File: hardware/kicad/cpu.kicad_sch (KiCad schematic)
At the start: 18 parts, among them U1 74AC04, U2 74AC245, U3 74AC573, U4 W65C816S, U5 DS1813-5+, X1 MXO45HS

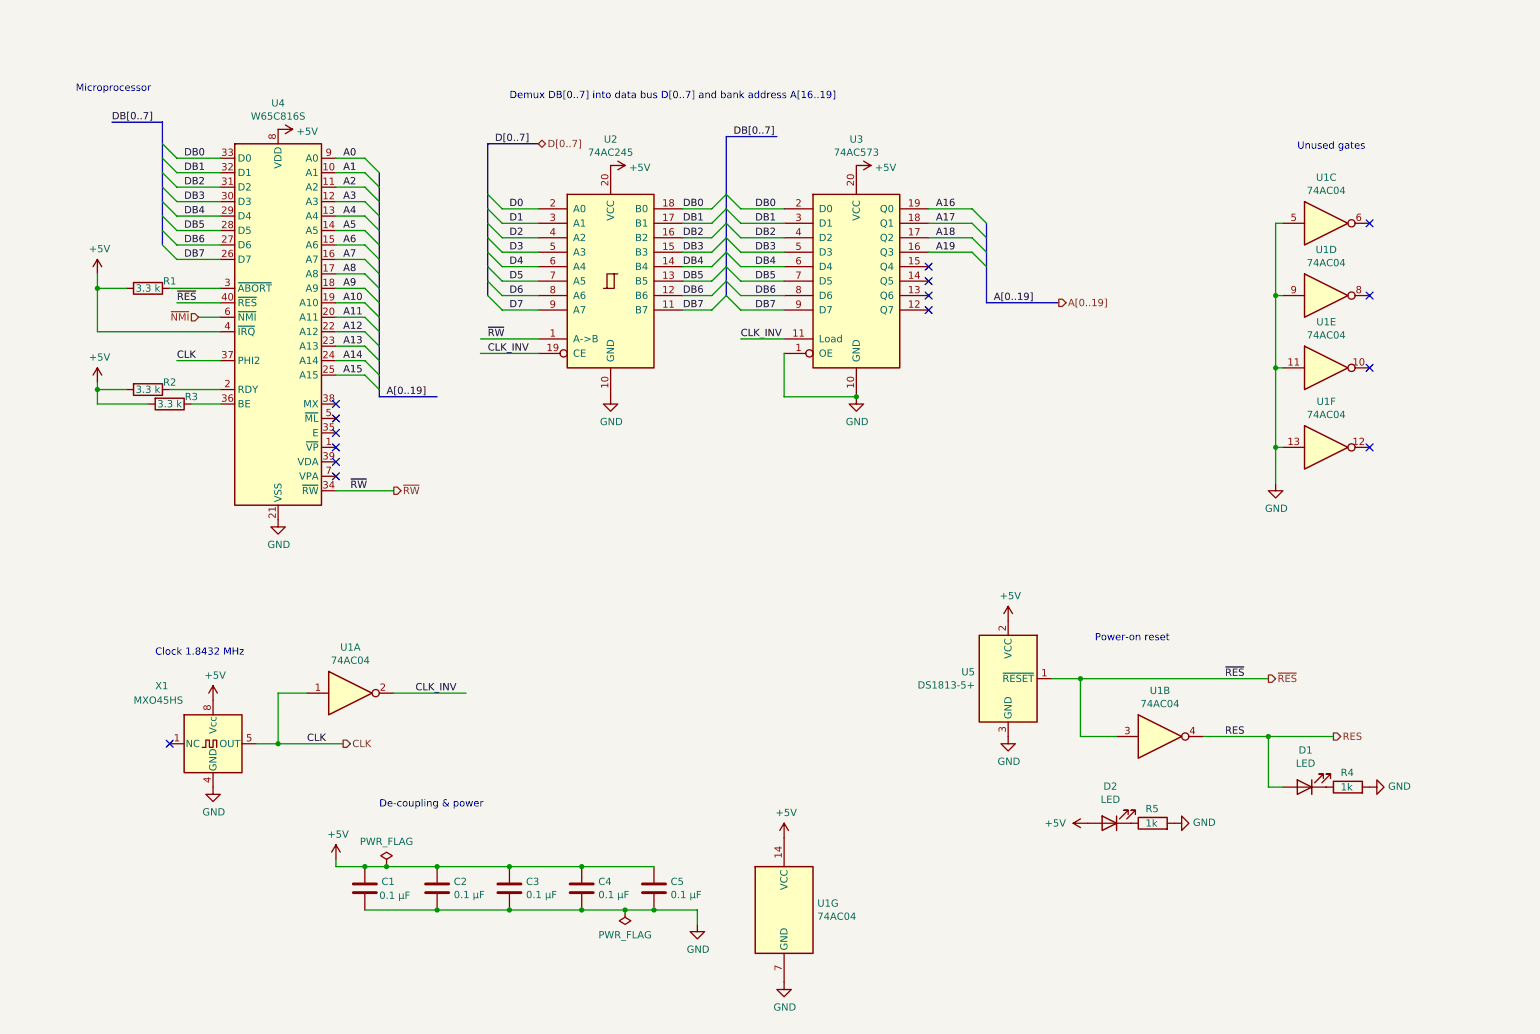
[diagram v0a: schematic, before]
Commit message: update hardware files to match current WIP design
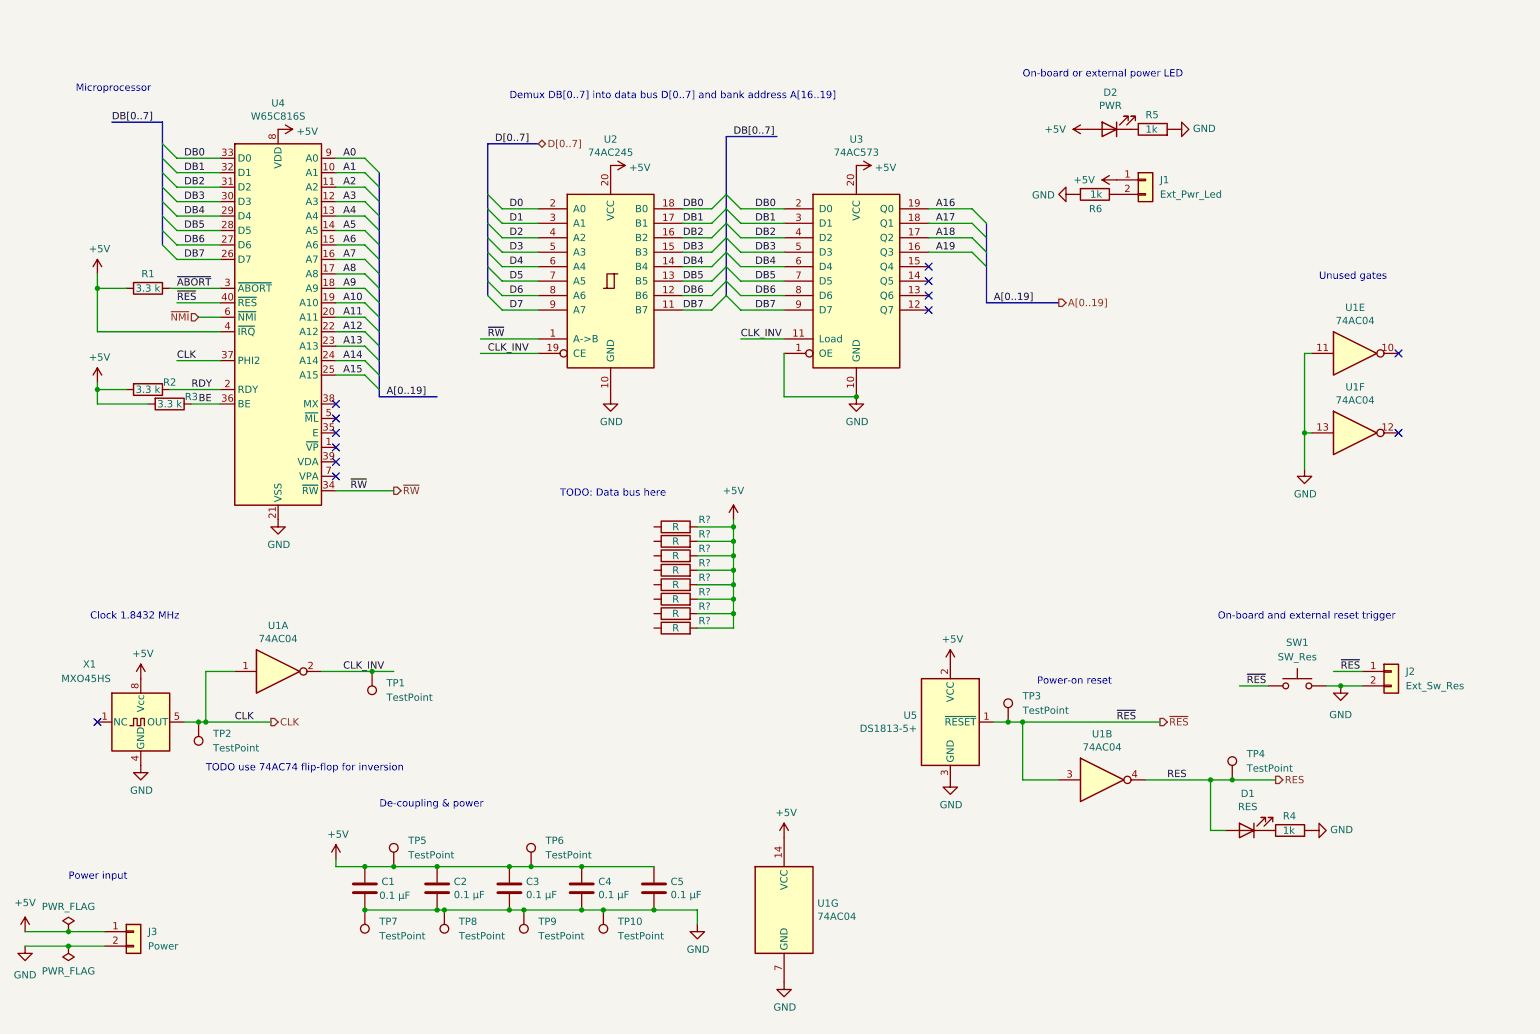
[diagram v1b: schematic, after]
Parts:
- removed unit 3 of U1
- removed unit 4 of U1
- added J1: Ext_Pwr_Led, Connector_PinHeader_2.54mm:PinHeader_1x02_P2.54mm_Vertical, symbol Connector_Generic:Conn_01x02
- added J2: Ext_Sw_Res, Connector_PinHeader_2.54mm:PinHeader_1x02_P2.54mm_Vertical, symbol Connector_Generic:Conn_01x02
- added J3: Power, Connector_PinHeader_2.54mm:PinHeader_1x02_P2.54mm_Vertical, symbol Connector_Generic:Conn_01x02
- added R6: 1k, Resistor_SMD:R_0603_1608Metric_Pad0.98x0.95mm_HandSolder, symbol Device:R
- added R? (x8): R, symbol Device:R
- added SW1: SW_Res, Button_Switch_THT:SW_TH_Tactile_Omron_B3F-10xx, symbol Switch:SW_Push
- added TP1, TP10, TP2, TP3, TP4, TP5, TP6, TP7, TP8, TP9: TestPoint, symbol Connector:TestPoint
- C1, C2, C3, C4, C5: footprint (none) -> Capacitor_SMD:C_0603_1608Metric_Pad1.08x0.95mm_HandSolder
- D1: value LED -> RES; footprint (none) -> LED_SMD:LED_0603_1608Metric_Pad1.05x0.95mm_HandSolder
- D2: value LED -> PWR; footprint (none) -> LED_SMD:LED_0603_1608Metric_Pad1.05x0.95mm_HandSolder
- R1, R2, R3, R4, R5: footprint (none) -> Resistor_SMD:R_0603_1608Metric_Pad0.98x0.95mm_HandSolder
- U1: footprint (none) -> Package_DIP:DIP-14_W7.62mm_Socket
- U2, U3: footprint (none) -> Package_DIP:DIP-20_W7.62mm_Socket
- U5: footprint Package_TO_SOT_SMD:SOT-23 -> Package_TO_SOT_THT:TO-92
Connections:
- net +5V: now also J1.1 (Pin_1), J3.1 (Pin_1), R?.2, R?.2, R?.2, R?.2, R?.2, R?.2, R?.2, R?.2, TP5.1, TP6.1
- net CLK: now also TP2.1
- net CLK_INV: now also TP1.1
- net GND: now also J2.2 (Pin_2), J3.2 (Pin_2), R6.2, SW1.2, TP10.1, TP7.1, TP8.1, TP9.1
- net RES: now also TP4.1
- net ~{RES}: now also J2.1 (Pin_1), SW1.1, TP3.1
- net RDY: now reaches R2.1, U4.2 (RDY)
- net ~{ABORT}: now reaches R1.1, U4.3 (~{ABORT})
- net BE: now reaches R3.1, U4.36 (BE)
- new net: J1.2 (Pin_2), R6.1
- no-connect marks 15 -> 13
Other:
- note added: "On-board and external reset trigger"
- note added: "On-board or external power LED"
- note added: "Power input"
- note added: "TODO use 74AC74 flip-flop for inversion"
- note added: "TODO: Data bus here"
- moved on the sheet: D1, D2, R4, R5, U1A, U1B, U1E, U1F, U5, X1

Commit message: update schematic, add draft PCB
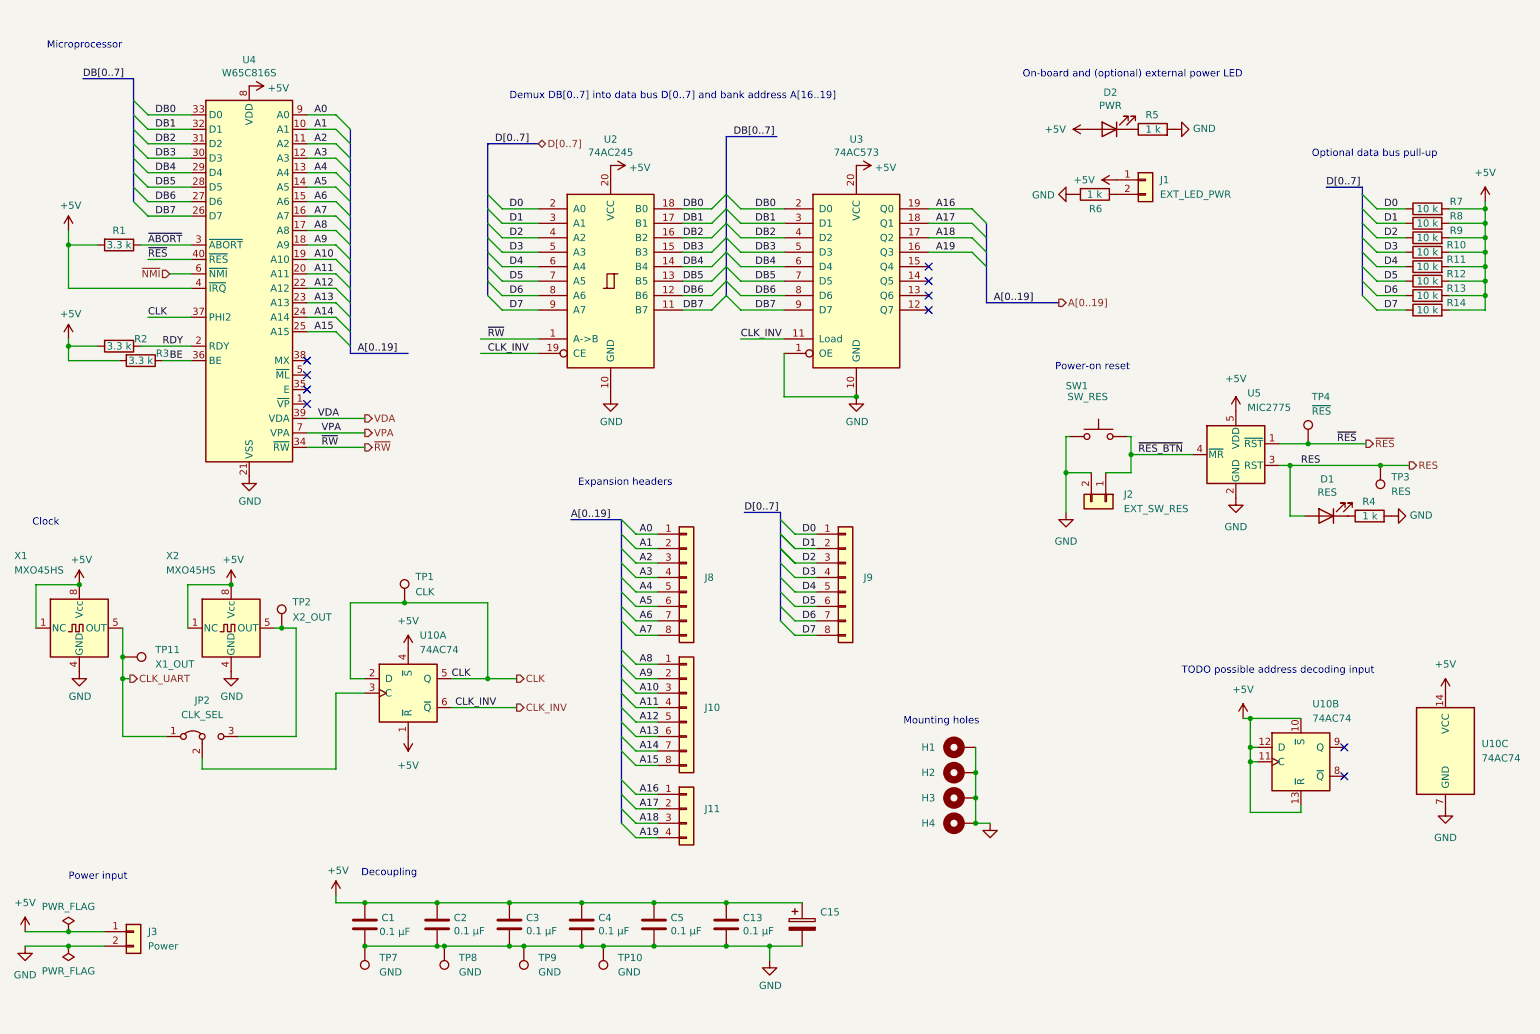
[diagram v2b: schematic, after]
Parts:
- removed TP5, TP6: TestPoint, symbol Connector:TestPoint
- removed U1: 74AC04, Package_DIP:DIP-14_W7.62mm_Socket, symbol project:74AC04
- removed U5: DS1813-5+, Package_TO_SOT_THT:TO-92, symbol project:DS1813-5+
- added C13: 0.1 µF, Capacitor_SMD:C_0603_1608Metric_Pad1.08x0.95mm_HandSolder, symbol Device:C
- added C15: (no value), symbol Device:C_Polarized
- added H1, H2, H3, H4: (no value), symbol Mechanical:MountingHole_Pad
- added J10, J8, J9: (no value), symbol Connector_Generic:Conn_01x08
- added J11: (no value), symbol Connector_Generic:Conn_01x04
- added JP2: CLK_SEL, Connector_PinHeader_2.54mm:PinHeader_1x03_P2.54mm_Vertical, symbol Jumper:Jumper_3_Bridged12
- added TP11: X1_OUT, TestPoint:TestPoint_Keystone_5005-5009_Compact, symbol Connector:TestPoint
- added U10: 74AC74, Package_DIP:DIP-14_W7.62mm_Socket, symbol project:74AC74
- added U5: MIC2775, Package_TO_SOT_SMD:SOT-23-5_HandSoldering, symbol project:MIC2775
- added X2: MXO45HS, Oscillator:Oscillator_DIP-8, symbol project:MXO45HS
- J1: value Ext_Pwr_Led -> EXT_LED_PWR
- J2: value Ext_Sw_Res -> EXT_SW_RES
- J3: footprint Connector_PinHeader_2.54mm:PinHeader_1x02_P2.54mm_Vertical -> Connector_JST:JST_XH_B2B-XH-A_1x02_P2.50mm_Vertical
- R10, R11, R12, R13, R14, R7, R8, R9: renamed from R?; value R -> 10 k; footprint (none) -> Resistor_SMD:R_0603_1608Metric_Pad0.98x0.95mm_HandSolder
- R4, R5, R6: value 1k -> 1 k
- SW1: value SW_Res -> SW_RES
- TP1: value TestPoint -> CLK; footprint (none) -> TestPoint:TestPoint_Keystone_5005-5009_Compact
- TP10, TP7, TP8, TP9: value TestPoint -> GND; footprint (none) -> TestPoint:TestPoint_Keystone_5005-5009_Compact
- TP2: value TestPoint -> X2_OUT; footprint (none) -> TestPoint:TestPoint_Keystone_5005-5009_Compact
- TP3: value TestPoint -> RES; footprint (none) -> TestPoint:TestPoint_Pad_D1.5mm
- TP4: value TestPoint -> ~{RES}; footprint (none) -> TestPoint:TestPoint_Keystone_5005-5009_Compact
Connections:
- net +5V: now also X1.1 (NC), C13.1, C15.1, U10.1 (~{R}), U10.10 (~{S}), U10.11 (C), U10.12 (D), U10.13 (~{R}), U10.14 (VCC), U10.4 (~{S}), U5.5 (VDD), X2.1 (NC), X2.8 (Vcc)
- net A0: now also J8.1 (Pin_1)
- net A1: now also J8.2 (Pin_2)
- net A10: now also J10.3 (Pin_3)
- net A11: now also J10.4 (Pin_4)
- net A12: now also J10.5 (Pin_5)
- net A13: now also J10.6 (Pin_6)
- net A14: now also J10.7 (Pin_7)
- net A15: now also J10.8 (Pin_8)
- net A16: now also J11.1 (Pin_1)
- net A17: now also J11.2 (Pin_2)
- net A18: now also J11.3 (Pin_3)
- net A19: now also J11.4 (Pin_4)
- net A2: now also J8.3 (Pin_3)
- net A3: now also J8.4 (Pin_4)
- net A4: now also J8.5 (Pin_5)
- net A5: now also J8.6 (Pin_6)
- net A6: now also J8.7 (Pin_7)
- net A7: now also J8.8 (Pin_8)
- net A8: now also J10.1 (Pin_1)
- net A9: now also J10.2 (Pin_2)
- net CLK: now also TP1.1, U10.2 (D), U10.5 (Q); no longer TP2.1, X1.5 (OUT)
- net CLK_INV: now also U10.6 (~{Q}); no longer TP1.1
- net D0: now also R7.1, J9.1 (Pin_1)
- net D1: now also R8.1, J9.2 (Pin_2)
- net D2: now also R9.1, J9.3 (Pin_3)
- net D3: now also R10.1, J9.4 (Pin_4)
- net D4: now also R11.1, J9.5 (Pin_5)
- net D5: now also R12.1, J9.6 (Pin_6)
- net D6: now also R13.1, J9.7 (Pin_7)
- net D7: now also R14.1, J9.8 (Pin_8)
- net GND: now also SW1.1, C13.2, C15.2, H1.1, H2.1, H3.1, H4.1, U10.7 (GND), U5.2 (GND), X2.4 (GND); no longer SW1.2
- net RES: now also TP3.1, U5.3 (RST); no longer TP4.1
- net ~{RES}: now also TP4.1, U5.1 (~{RST}); no longer J2.1 (Pin_1), SW1.1, TP3.1
- net VDA: now reaches U4.39 (VDA)
- net VPA: now reaches U4.7 (VPA)
- new net: JP2.2 (C), U10.3 (C)
- new net: JP2.3 (B), TP2.1, X2.5 (OUT)
- new net CLK_UART: JP2.1 (A), TP11.1, X1.5 (OUT)
- new net ~{RES_BTN}: J2.1 (Pin_1), SW1.2, U5.4 (~{MR})
- no-connect marks 13 -> 10
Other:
- note added: "Clock"
- note added: "Decoupling"
- note added: "Expansion headers"
- note added: "Mounting holes"
- note added: "On-board and (optional) external power LED"
- note added: "Optional data bus pull-up"
- note added: "TODO possible address decoding input"
- note removed: "Clock 1.8432 MHz"
- note removed: "De-coupling & power"
- note removed: "On-board and external reset trigger"
- note removed: "On-board or external power LED"
- note removed: "TODO use 74AC74 flip-flop for inversion"
- note removed: "TODO: Data bus here"
- note removed: "Unused gates"
- moved on the sheet: C1, C2, C3, C4, C5, D1, J2, R1, R10, R11, R12, R13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

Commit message: pcb updates
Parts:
- added D3: EMU, LED_SMD:LED_0603_1608Metric_Pad1.05x0.95mm_HandSolder, symbol Device:LED
- added J13, J14: Conn_01x06, Connector_PinHeader_2.54mm:PinHeader_1x06_P2.54mm_Vertical, symbol Connector_Generic:Conn_01x06
- added JP4: Jumper_2_Bridged, Connector_PinHeader_2.54mm:PinHeader_1x02_P2.54mm_Vertical, symbol Jumper:Jumper_2_Bridged
- added JP5: SolderJumper_2_Open, Jumper:SolderJumper-2_P1.3mm_Open_RoundedPad1.0x1.5mm, symbol Jumper:SolderJumper_2_Open
- added R17: 1 k, Resistor_SMD:R_0603_1608Metric_Pad0.98x0.95mm_HandSolder, symbol Device:R
- added TP5, TP6: (no value), TestPoint:TestPoint_Keystone_5005-5009_Compact, symbol Connector:TestPoint
- added U14: DS1813-5+, Package_TO_SOT_THT:TO-92_Inline, symbol project:DS1813-5+
- C15: value (none) -> 100 µF; footprint (none) -> Capacitor_THT:CP_Radial_D6.3mm_P2.50mm
- H1, H2, H3, H4: value (none) -> MountingHole_Pad; footprint (none) -> MountingHole:MountingHole_3.2mm_M3_Pad_Via
- J10, J8, J9: value (none) -> Conn_01x08; footprint (none) -> Connector_PinHeader_2.54mm:PinHeader_1x08_P2.54mm_Vertical
- J11: value (none) -> Conn_01x04; footprint (none) -> Connector_PinHeader_2.54mm:PinHeader_1x04_P2.54mm_Vertical
- U4: footprint Package_DIP:DIP-40_W15.24mm -> Package_DIP:DIP-40_W15.24mm_Socket
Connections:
- net +5V: now also JP4.2 (B), U14.2 (VCC); no longer U4.4 (~{IRQ})
- net BE: now also J14.6 (Pin_6)
- net GND: now also R17.2, U14.3 (GND)
- net RDY: now also J14.2 (Pin_2)
- net VDA: now also J13.4 (Pin_4)
- net VPA: now also J13.5 (Pin_5)
- net ~{ABORT}: now also J14.4 (Pin_4)
- net ~{NMI}: now also J14.5 (Pin_5), TP6.1
- net ~{RES_BTN}: now also JP5.1 (A), U14.1 (~{RESET})
- net ~{RES}: now also J14.3 (Pin_3), JP5.2 (B)
- net ~{RW}: now also J13.6 (Pin_6)
- net ~{VP}: now reaches U4.1 (~{VP})
- net ~{VP}: now also J14.1 (Pin_1)
- net EMU: now reaches U4.35 (E)
- net EMU: now also D3.2 (A), J13.3 (Pin_3)
- net MX: now reaches U4.38 (MX)
- net MX: now also J13.1 (Pin_1)
- net ~{ML}: now reaches U4.5 (~{ML})
- net ~{ML}: now also J13.2 (Pin_2)
- new net: D3.1 (K), R17.1
- new net ~{IRQ}: JP4.1 (A), TP5.1, U4.4 (~{IRQ})
- no-connect marks 10 -> 6
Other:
- note added: "Alternative, bridge jumper if used"
- note added: "Emulation LED"
- note added: "External IRQ input, connect to VCC if not used"
- note added: "Unused flip-flop"
- note removed: "TODO possible address decoding input"
- moved on the sheet: D1, D2, H1, H2, H3, H4, J1, J2, R10, R11, R12, R13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

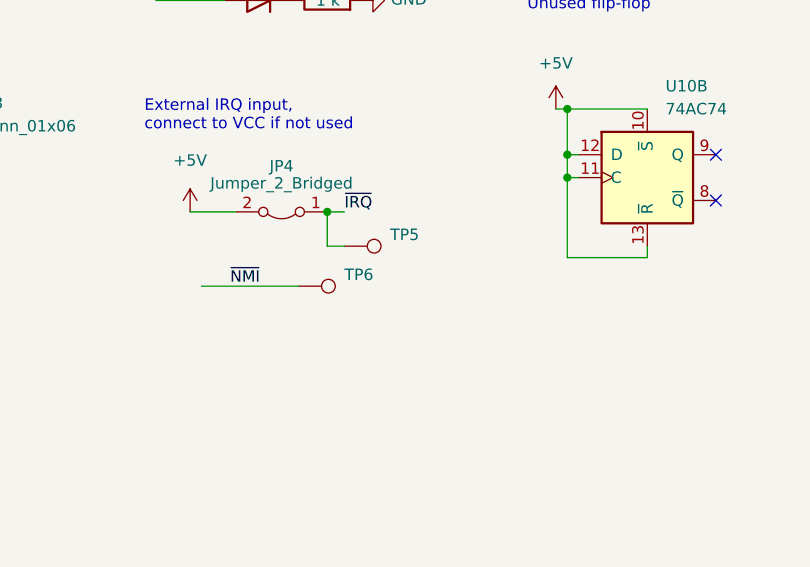
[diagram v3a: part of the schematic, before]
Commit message: add gerbers for test board
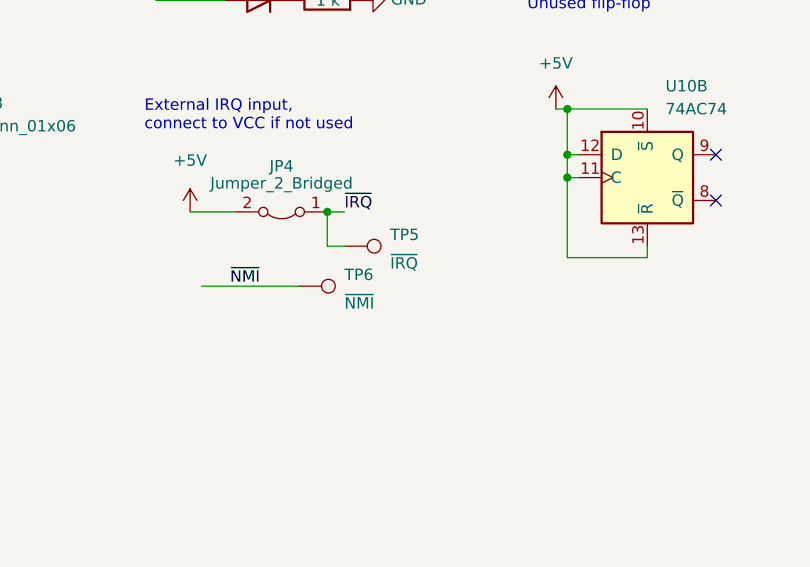
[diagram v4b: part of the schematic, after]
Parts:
- TP5: value (none) -> ~{IRQ}
- TP6: value (none) -> ~{NMI}
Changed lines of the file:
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@@
       (effects (font (size 1.27 1.27)) (justify left))
     )
-    (property "Value" "" (id 1) (at 208.28 161.9249 90)
+    (property "Value" "~{NMI}" (id 1) (at 208.28 161.9249 90)
       (effects (font (size 1.27 1.27)) (justify left))
     )
@@
       (effects (font (size 1.27 1.27)) (justify left))
     )
-    (property "Value" "" (id 1) (at 213.36 157.4799 90)
-      (effects (font (size 1.27 1.27)) (justify left))
-    )
+    (property "Value" "~{IRQ}" (id 1) (at 213.36 157.4799 90)
+      (effects (font (size 1.27 1.27)) (justify left))
+    )
